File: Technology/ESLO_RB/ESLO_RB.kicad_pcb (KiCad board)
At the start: 4 copper layers, 27 x 13 mm, 65 parts, among them CN1 4700pF, CN2 1000pF, CN3 1000pF, CN4 1uF, CN5 1uF, J1 10POS Biopotentials, J2 6POS Power/JTAG, U1 MAX1720, U10 2450BM14G0011, U2 TPS62740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

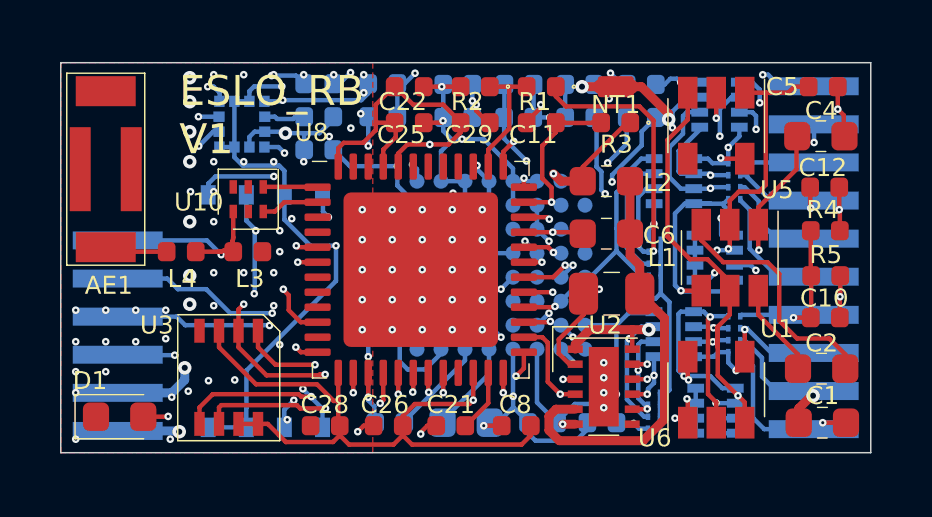
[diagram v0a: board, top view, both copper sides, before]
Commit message: Debugging ESLO PBCs
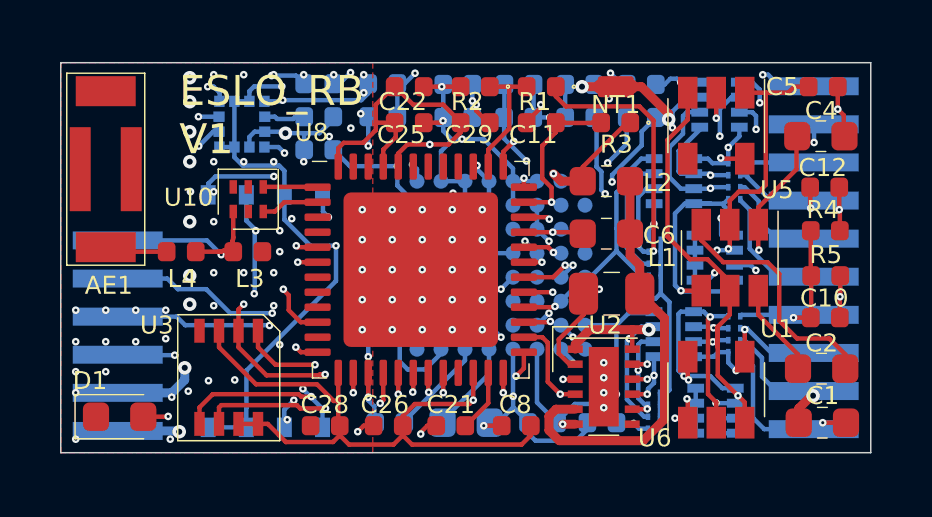
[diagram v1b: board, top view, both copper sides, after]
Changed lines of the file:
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@@
     (1 GNDD power hide)
     (2 VSSA power hide)
-    (31 B.Cu mixed)
+    (31 B.Cu mixed hide)
     (32 B.Adhes user hide)
     (33 F.Adhes user hide)
@@
     (35 F.Paste user hide)
     (36 B.SilkS user)
-    (37 F.SilkS user hide)
+    (37 F.SilkS user)
     (38 B.Mask user hide)
     (39 F.Mask user hide)
@@
     (at 130.75 94.25)
     (attr smd)
-    (fp_text reference U10 (at -1.65 0.1 180) (layer F.SilkS)
+    (fp_text reference U10 (at -1.99 -0.06 180) (layer F.SilkS)
       (effects (font (size 0.6 0.6) (thickness 0.07)))
     )
